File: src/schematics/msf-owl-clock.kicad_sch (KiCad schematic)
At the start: 14 parts, among them U001 BC805M

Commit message: Elaboration of the top-level schematicd.
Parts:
- added C21, C22: 10μF, restall-generic-capacitors:unpolarised-nominal-0805-2012, symbol restall-generic-capacitors:capacitor-unpolarised
- added D001, D002, D003, D004, D005, D006, D007, D1: D5V0FS4U10LP, restall-manufacturer-diodes-inc:D5V0FS4U10LP, symbol restall-manufacturer-diodes-inc:D5V0FS4U10LP
- added FB001: WLBD1608HCU102TH, restall-manufacturer-walsin:WLBD1608, symbol restall-manufacturer-walsin:WLBD1608HCU102TH
- added R301 (x7): ??Ω, restall-generic-resistors:nominal-0402-1005, symbol restall-generic-resistors:resistor
- added R301: ??kΩ, restall-generic-resistors:nominal-0402-1005, symbol restall-generic-resistors:resistor
- added R301 (x2): 330Ω, restall-generic-resistors:nominal-0402-1005, symbol restall-generic-resistors:resistor
- added R301 (x3): 10kΩ, restall-generic-resistors:nominal-0402-1005, symbol restall-generic-resistors:resistor
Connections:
- net 3-mcu-core/MCU_V{DD}: now also R301.2
- net CC1: now also D002.1 (K)
- net CC2: now also D002.2 (K)
- net CLK: now also D006.4 (K)
- net CMD: now also D006.5 (K)
- net DAT0: now also D006.2 (K)
- net DAT1: now also D006.1 (K)
- net DAT2: now also D007.2 (K)
- net DAT3: now also D007.1 (K)
- net D_{+}: now also D002.5 (K)
- net D_{-}: now also D002.4 (K)
- net GND: now also U001.8 (GND), C21.2, C22.2, D001.3 (A), D001.3 (A), D001.3 (A), D001.8 (A), D001.8 (A), D001.8 (A), D002.3 (A), D002.3 (A), D002.3 (A), D002.3 (A), D002.8 (A), D002.8 (A), D002.8 (A), D002.8 (A), D003.3 (A), D003.3 (A), D003.3 (A), D003.3 (A), D003.8 (A), D003.8 (A), D003.8 (A), D003.8 (A), D004.3 (A), D004.3 (A), D004.3 (A), D004.3 (A), D004.8 (A), D004.8 (A), D004.8 (A), D004.8 (A), D005.3 (A), D005.3 (A), D005.3 (A), D005.3 (A), D005.8 (A), D005.8 (A), D005.8 (A), D005.8 (A), D006.3 (A), D006.3 (A), D006.3 (A), D006.3 (A), D006.8 (A), D006.8 (A), D006.8 (A), D006.8 (A), D007.3 (A), D007.3 (A), D007.3 (A), D007.3 (A), D007.8 (A), D007.8 (A), D007.8 (A), D007.8 (A), D1.3 (A), D1.8 (A), R301.2
- net at CONN003.1 (V_{CC}): now also R301.1
- net at CONN003.10 (~{RESET}), U001.4 (P021): now also D001.4 (K), R301.1
- net at CONN003.2 (SWDIO): now also D001.1 (K), R301.1, R301.2; no longer U001.1 (SWDIO)
- net at CONN003.4 (SWCLK): now also D001.2 (K), R301.1, R301.1; no longer U001.2 (SWCLK)
- net at CONN003.6 (SWO): now also R301.2
- net at CONN004.1 (V_{CC}): now also R301.1
- net ~{RESET}: now reaches CONN004.10 (~{RESET})
- net ~{RESET}: now also D005.1 (K), R301.2
- net TRACECLK: now reaches CONN004.12 (TRACECLK)
- net TRACECLK: now also D004.1 (K)
- net TRACEDATA0: now reaches CONN004.14 (TRACEDATA[0])
- net TRACEDATA0: now also D003.5 (K)
- net TRACEDATA1: now reaches CONN004.16 (TRACEDATA[1])
- net TRACEDATA1: now also D003.4 (K)
- net TRACEDATA2: now reaches CONN004.18 (TRACEDATA[2])
- net TRACEDATA2: now also D003.2 (K)
- net SWDIO: now reaches CONN004.2 (SWDIO)
- net SWDIO: now also U001.1 (SWDIO), D005.5 (K), R301.2
- net TRACEDATA3: now reaches CONN004.20 (TRACEDATA[3])
- net TRACEDATA3: now also D003.1 (K)
- net SWCLK: now reaches CONN004.4 (SWCLK)
- net SWCLK: now also U001.2 (SWCLK), D005.4 (K), R301.2
- net SWO: now reaches CONN004.6 (SWO)
- net SWO: now also D005.2 (K)
- net ~{RTS}: now reaches U001.10 (P005)
- net at U001.11 (P014): now also R301.1
- net TXD: now reaches U001.12 (P004)
- net SDA: now reaches U001.13 (P000)
- net SCL: now reaches U001.14 (P001)
- net at U001.3 (P020): now also R301.2
- net at U001.5 (P018): now also R301.2
- net at U001.6 (P016): now also R301.2
- net at U001.7 (P012): now also R301.2
- net BC805M_V_{DD}: now reaches U001.9 (VDD)
- net BC805M_V_{DD}: now also C21.1, C22.1, D1.5 (K), FB001.1 (P1), R301.1, R301.1, R301.2
- net CD renamed ~{CD}
- net ~{CD}: now also D007.5 (K)
- net SBU1: no longer names the net of CONN001.A8 (SBU1)
- net SBU2: no longer names the net of CONN001.B8 (SBU2)
- net WP renamed ~{WP}
- net ~{WP}: now also D007.4 (K)
- new net MISO: R301.1
- new net MOSI: R301.1
- new net RXD: R301.2
- new net SCK: R301.1
- new net ~{CTS}: R301.1
- no-connect marks 1 -> 2
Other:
- sheet 1-usb-and-power ports: added {PWR_FLAGS}, {USB_BC_FLAGS}, {USB_DATA}, ~{USB_PD_INT}; removed {USBC_MCU}, ~{USB_PWRFAULT}
- sheet 2-msf-receiver ports: added MSF_RCV_{+3.3V_IO}, MSF_RCV_{+5V}, {MSF_RCV_GAINS}; removed MSF_REC_{+3.3V_IO}, MSF_REC_{+5V}, {MSF_REC_GAINS}
- sheet 3-mcu-core ports: added MSF_RCV_EN, {BC805M_SPI}, {BC805M_UART}, {IR_RCV}, {MSF_RCV_GAINS}, {PWR_FLAGS}, {SENSOR_FLAGS}, {USB_BC_FLAGS}, {USB_DATA}, ~{USB_PD_INT}; removed MSF_REC_EN, {MSF_REC_GAINS}, {SPI}, {USBC_MCU}, ~{USB_PWRFAULT}
- sheet 5-sensors ports: added {I^{2}C}, {SENSOR_FLAGS}; removed none
- note added: "47uF 10V Tant Poly 70m-ohm 1411 £0.41 - T55B476M010C0070 100uF 16V Alu Poly 6.6mm x 6.6mm £0.16 - SVL1CM101E06E00RS153 (better MTBF - 10000h @ 105C) 47uF 10V X7R MLCC 1210 £0.49 - GRM32ER71A476ME15K"
- note added: "D001A-C"
- note added: "D002A-D"
- note added: "D003A-D"
- note added: "D004B-D"
- note added: "D005A-D"
- note added: "D006A-D"
- note added: "D007A-D"
- note added: "R003-4"
- note added: "R00?-?"
- note added: "TODO: 0402 bypass, too"
- note added: "TODO: BC805M pin assignments for SPI, I^{2}C and UART are flexible depending if layout demands it. SPI is the fastest, expected at bursts up to 16MHz. UART next at up to 1MHz, followed by I^{2}C at 400kHz."
- note added: "TODO: NOTE ABOUT ALL R AND C BEING 0402 UNLESS SPECIFIED. ALSO ALL R THICK FILM 1% 100ppm. ALSO ALL C MLCC +/- 10% X5R 16V."
- note added: "TODO: USE TSOP75338TT(to 3-mcu via UART) FOR 38kHz IR RECEIVER (500uA current) - MAKE THIS TOGGLEABLE (SUPPLIED BY AN I/O PIN) TO SAVE ON CURRENT IN STANDBY MODE (IE. NO REMOTE WAKEUP BY IR)"
- note added: "TODO: WIRE TO MCU V_{DD}"
- note added: "UART pins named from the MCU perspective"
- note removed: "SERCOM0,5,2,1|3,4,6,7 7x serial - SPI to BC805M I2C to BC805M UART to BC805M UART to TPS (infrared) I2C to sensors I2C to FUSB302 I2C to TFTs SDHC1 to SD card QSPI to TFTs IN REALITY, ONLY ONE I2C IS AVAILABLE (SERCOM3)."
- note removed: "TODO: 2x TFT connectors (to 6-tft)"
- note removed: "TODO: BCM805M SERIES TERMINATOR ON SWDIO FOR MCU ?"
- note removed: "TODO: BUS CONN003 SWDIO AND SWCLK TO THE PIC32 FOR ICSP."
- note removed: "TODO: SWO IS N/C - IS THIS CORRECT, OR DOES IT NEED A PULL ?"
- note removed: "TODO: USE SINGLE-ENDED DAC AND USE THE OTHER DAC FOR SOMETHING ELSE, SUCH AS A VCO, A TEST SIGNAL OR A REFERENCE SIGNAL ? IF DAC0 IS FREED UP THEN THAT CAN ALSO BE AN INPUT INTO AN ADC."
- note removed: "TODO: USE TSOP75338TT(to 3-mcu via UART) FOR 38kHz IR RECEIVER (500uA current) - MAKE THIS TOGGLEABLE (MAYBE SUPPLIED BY AN I/O PIN ?) TO SAVE ON CURRENT IN STANDBY MODE (NO REMOTE WAKEUP BY IR) IR TRANSMITTER - B1701IR--20C000114U1930, 940nm, If=65mA, 140deg, 0805, Vf=1.5V - note that USART line idles high, so need an inverter for the transmitter."
- note removed: "TODO: VCC VIA RESISTOR ?"
- moved on the sheet: ANT001, C001, C002, C003, CONN005, CONN006, LED001, R4, SPK001, U001

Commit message: Further elaboration of the design and schematics, mainly power supply calculations.
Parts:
- C21: value 10μF -> 22μF; Label 10μF±10% 16V X5R -> 22μF±20% 10V X5R; ManufacturerPartNumber CL21A106KOQNNNE -> CL21A226MPQNNN; Tolerance ±10% -> ±20%; VoltageRating 16V -> 10V
- C22: value 10μF -> DNP; Label 10μF±10% 16V X5R -> 22μF±20% 10V X5R; ManufacturerPartNumber CL21A106KOQNNNE -> CL21A226MPQNNN; Tolerance ±10% -> ±20%; VoltageRating 16V -> 10V; now left out of the parts list
- renumbered R4 to R001, R301 to R001, R301 to R002, R301 to R003, R301 to R004, R301 to R005, R301 to R006, R301 to R14, R301 to R15, R301 to R16, R301 to R17, R301 to R18, R301 to R19, R301 to R20
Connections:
- net BC805M_V_{DD}: now also FB001.2 (P2); no longer FB001.1 (P1)
- net 3-mcu-core/MCU_V{DD} renamed 1-usb-and-power/CORE_VDD_{+3.3V}
- net 1-usb-and-power/CORE_VDD_{+3.3V}: now also FB001.1 (P1)
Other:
- sheet 1-usb-and-power ports: added CORE_VDD_MODE, CORE_VDD_{+3.3V}, CORE_VDD_{+5V}; removed none
- sheet 2-msf-receiver ports: added CORE_VDD_{+5V}, MSF_RCV_EN; removed MSF_RCV_{+5V}
- sheet 3-mcu-core ports: added CORE_VDD_MODE, CORE_VDD_{+3.3V}; removed MCU_V{DD}
- sheet 4-audio-out ports: added CORE_VDD_{+5V}; removed AUDIO_AMP_{+5V}
- note added: "POWER DOMAINS: USB VBUS -> BUCK 3.3V, 2A (~2.25MHz) - TPS628512 (is L current acceptable for USB specs ?) -> USB SUPPORT (FUSB302, ETC.) MCU BC805M TFT LDO 2.8V -> SENSORS LOAD SWITCH -> SD Card LOAD SWITCH -> Audio LDO 3.6V -> MSF RECEIVER"
- note added: "TODO: 60x 4.7uF 0402 bypass caps plus 22uF bulk next to BC805M = about maximum C for the +3.3V line."
- note added: "TODO: NOISE OF AZ431L MAY NOT BE LOW ENOUGH - NO NOISE FIGURES GIVEN IN DATASHEET. MAYBE EVEN ANOTHER (HIGHER-Z) REFERENCE WITH AN OPAMP BUFFER WOULD BE BETTER ?"
- note added: "TODO: NOTE ABOUT ALL R AND C BEING 0402 UNLESS SPECIFIED. ALSO ALL R THICK FILM 1% 100ppm. ALSO ALL C MLCC +/- 10% X5R 10V."
- note added: "TODO: VREF WITH NOISE < 315nV/sqrt(Hz) REQUIRED FOR 16-BIT RESOLUTION IN 100Hz BANDWIDTH; P458 OF 'DATA CONVERTERS'."
- note removed: "POWER DOMAINS: USB VBUS -> BUCK 3.3V, 1.5A (~1MHz ?) - AP62150 (is VUSB always >= 4.2V ? Is L current acceptable for USB specs ?) -> USB SUPPORT (FUSB302, ETC.) MCU BC805M TFT LDO 2.8V -> SENSORS LOAD SWITCH -> SD Card LOAD SWITCH -> Audio LDO 3.6V -> MSF RECEIVER"
- note removed: "TODO: 0402 bypass, too"
- note removed: "TODO: BC805M Bluetooth module (to 3-mcu). VDD-GND needs > 47uF bypass."
- note removed: "TODO: BUDGET 1mA FOR PROXIMITY SENSOR IN SLEEP WHEN USB SUSPENDED (MAX 2.5mA DRAW FROM ALL CIRCUITRY), 500uA AT A PUSH - p26. MCU BUDGET FOR AROUND 600uA IN STANDBY BUDGET 500uA FOR INFRARED RECEIVER BUDGET 222uA FOR USB PULL-UP PLUS ALL LEAKAGE FROM CAPS, LDOs, FUSB303, USB PULL-UP / DOWN, ETC. ETC. BLUETOOTH IS TOO HUNGRY (ABOUT 10mA RECEIVE CURRENT) TO LISTEN DURING USB SUSPEND. CHECK THESE FI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"
- note removed: "TODO: NOTE ABOUT ALL R AND C BEING 0402 UNLESS SPECIFIED. ALSO ALL R THICK FILM 1% 100ppm. ALSO ALL C MLCC +/- 10% X5R 16V."
- note removed: "TODO: WIRE TO MCU V_{DD}"
- moved on the sheet: C21, FB001, SPK001

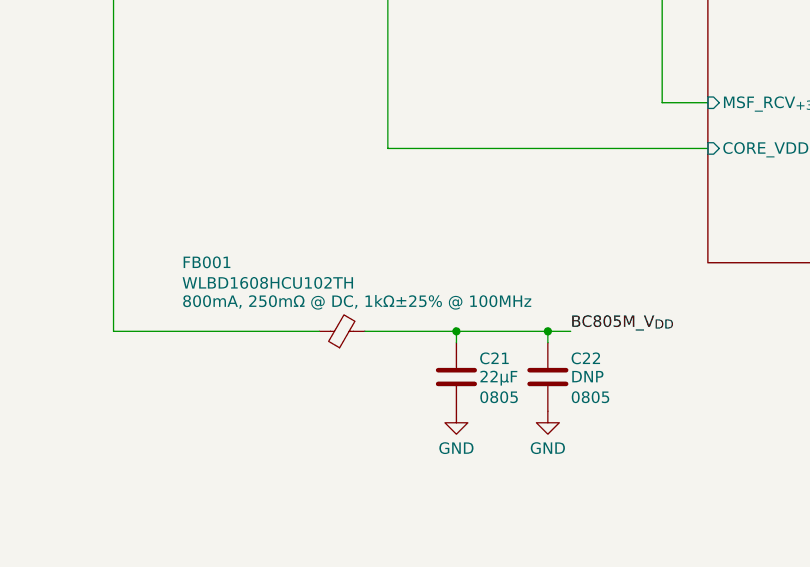
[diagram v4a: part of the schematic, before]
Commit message: Started to draw the USB / power input module.
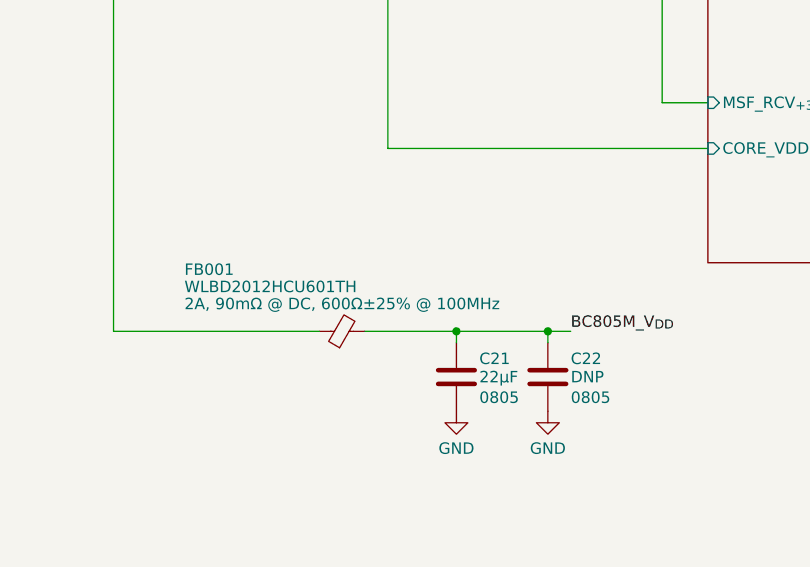
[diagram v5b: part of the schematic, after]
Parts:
- removed FB001: WLBD1608HCU102TH, restall-manufacturer-walsin:WLBD1608, symbol restall-manufacturer-walsin:WLBD1608HCU102TH
- added FB001: WLBD2012HCU601TH, restall-manufacturer-walsin:WLBD2012, symbol restall-manufacturer-walsin:WLBD2012HCU601TH
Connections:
- net 1-usb-and-power/CORE_VDD_{+3.3V}: now also FB001.1 (P1)
- net BC805M_V_{DD}: now also FB001.2 (P2)
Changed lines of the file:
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@@
-    )
-  )
-  (symbol (lib_id "restall-manufacturer-walsin:WLBD1608HCU102TH") (at 182.88 228.6 90) (unit 1)
-    (in_bom yes) (on_board yes) (dnp no)
-    (property "Reference" "FB001" (at 165.1 220.98 90)
-      (effects (font (size 1.27 1.27)) (justify right))
-    )
-    (property "Value" "WLBD1608HCU102TH" (at 165.1 223.266 90)
-      (effects (font (size 1.27 1.27)) (justify right))
-    )
-    (property "Footprint" "restall-manufacturer-walsin:WLBD1608" (at 182.88 230.378 90)
-      (effects (font (size 1.27 1.27)) (justify right) hide)
-    )
-    (property "Datasheet" "https://www.passivecomponent.com/wp-content/uploads/inductor/WLBD1005-4532_HC.pdf" (at 200.406 226.568 0)
-      (effects (font (size 1.27 1.27)) (justify left) hide)
-    )
-    (property "Label" "800mA, 250mΩ @ DC, 1kΩ±25% @ 100MHz" (at 165.1 225.298 90)
-      (effects (font (size 1.27 1.27)) (justify right))
-    )
-    (property "DCR" "250mΩ" (at 192.278 226.568 0)
-      (effects (font (size 1.27 1.27)) (justify left) hide)
-    )
-    (property "I_{MAX}" "800mA" (at 190.246 226.568 0)
-      (effects (font (size 1.27 1.27)) (justify left) hide)
-    )
-    (property "Impedance" "1kΩ @ 100MHz" (at 194.31 226.568 0)
-      (effects (font (size 1.27 1.27)) (justify left) hide)
-    )
-    (property "Tolerance" "±25%" (at 196.342 226.822 0)
-      (effects (font (size 1.27 1.27)) (justify left) hide)
-    )
-    (property "Manufacturer" "Walsin Technology" (at 198.374 226.568 0)
-      (effects (font (size 1.27 1.27)) (justify left) hide)
-    )
-    (property "ManufacturerPartNumber" "WLBD1608HCU102TH" (at 186.182 226.568 0)
-      (effects (font (size 1.27 1.27)) (justify left) hide)
-    )
-    (pin "2")
-    (pin "1")
-    (instances
-      (project "msf-owl-clock"
-        (path "/56d623d3-22db-4d43-a9d9-e6bb4bb68946"
-          (reference "FB001") (unit 1)
-        )
-      )
     )
   )
@@
         )
       )
+    )
+  )
+  (symbol (lib_id "restall-manufacturer-walsin:WLBD2012HCU601TH") (at 182.88 228.6 90) (unit 1)
+    (in_bom yes) (on_board yes) (dnp no)
+    (property "Reference" "FB001" (at 165.354 221.742 90)
+      (effects (font (size 1.27 1.27)) (justify right))
+    )
+    (property "Value" "WLBD2012HCU601TH" (at 165.354 223.6582 90)
+      (effects (font (size 1.27 1.27)) (justify right))
+    )
+    (property "Footprint" "restall-manufacturer-walsin:WLBD2012" (at 182.88 230.378 90)
+      (effects (font (size 1.27 1.27)) (justify right) hide)
+    )
+    (property "Datasheet" "https://www.passivecomponent.com/wp-content/uploads/inductor/WLBD1005-4532_HC.pdf" (at 200.406 226.568 0)
+      (effects (font (size 1.27 1.27)) (justify left) hide)
+    )
+    (property "Label" "2A, 90mΩ @ DC, 600Ω±25% @ 100MHz" (at 165.354 225.552 90)
+      (effects (font (size 1.27 1.27)) (justify right))
+    )
+    (property "DCR" "90mΩ" (at 192.278 226.568 0)
+      (effects (font (size 1.27 1.27)) (justify left) hide)
+    )
+    (property "I_{MAX}" "2A" (at 190.246 226.568 0)
+      (effects (font (size 1.27 1.27)) (justify left) hide)
+    )
+    (property "Impedance" "600Ω @ 100MHz" (at 194.31 226.568 0)
+      (effects (font (size 1.27 1.27)) (justify left) hide)
+    )
+    (property "Tolerance" "±25%" (at 196.342 226.822 0)
+      (effects (font (size 1.27 1.27)) (justify left) hide)
+    )
+    (property "Manufacturer" "Walsin Technology" (at 198.374 226.568 0)
+      (effects (font (size 1.27 1.27)) (justify left) hide)
+    )
+    (property "ManufacturerPartNumber" "WLBD2012HCU601TH" (at 186.182 226.568 0)
+      (effects (font (size 1.27 1.27)) (justify left) hide)
+    )
+    (pin "1")
+    (pin "2")
+    (instances
+      (project "msf-owl-clock"
+        (path "/56d623d3-22db-4d43-a9d9-e6bb4bb68946"
+          (reference "FB001") (unit 1)
+        )
+      )
